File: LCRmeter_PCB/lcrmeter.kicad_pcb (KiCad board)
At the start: 2 copper layers, 64 x 55.2 mm, 70 parts, among them IC1 TPS2116DRLR, J1 LCR_input, J2 LCR_input, J3 Prog_interface, J4 USB_B_Micro, J6 misc, J7 misc, Q1 NX7002BKR, SW1 power, SW2 up, SW3 down, SW4 ok, SW5 back, U1 74LVC1G66, U10 MCP6001-OT, U2 74LVC1G66, U3 OLED, U4 74HC14, U5 MCP6001-OT, U6 STM32G473C_B-C-E_Tx, U7 74LVC1G66, U8 MCP6001-OT, U9 LM1117MP-3.3

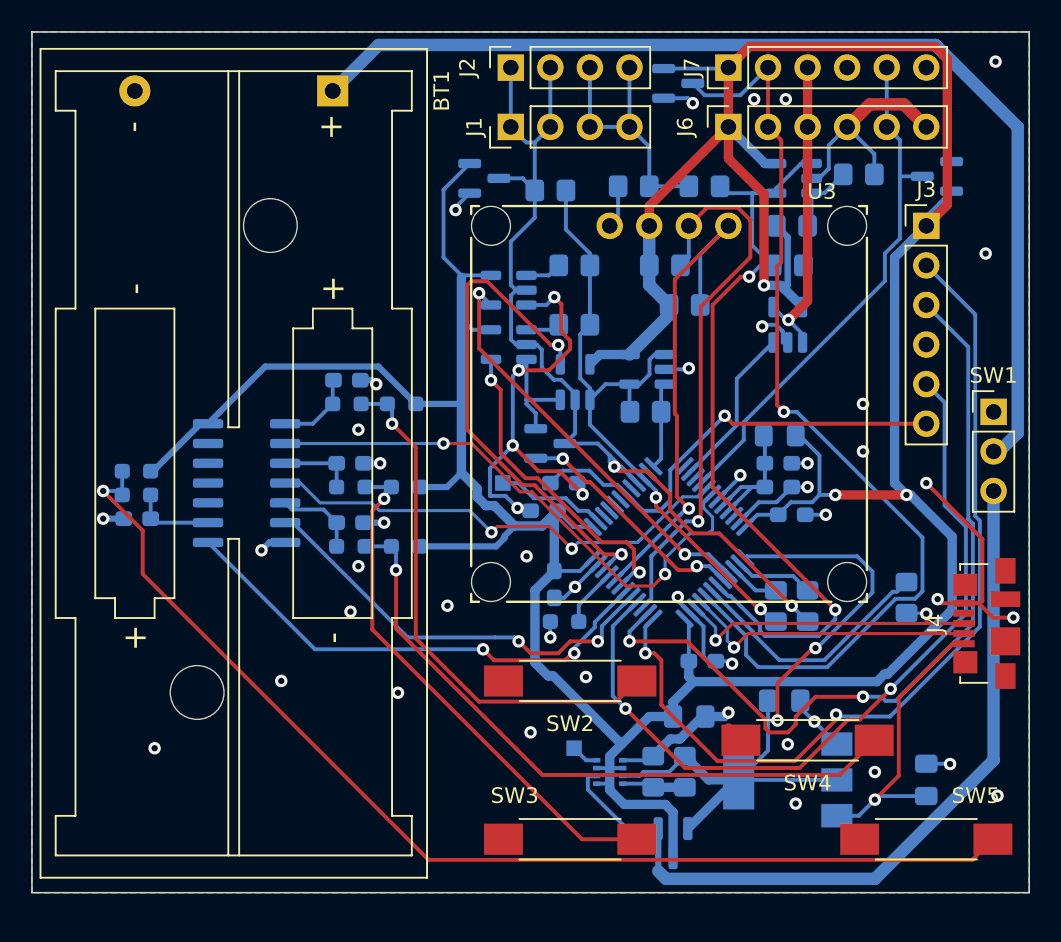
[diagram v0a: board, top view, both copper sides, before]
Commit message: Fix TG connection for Vg; component placement; filter basis
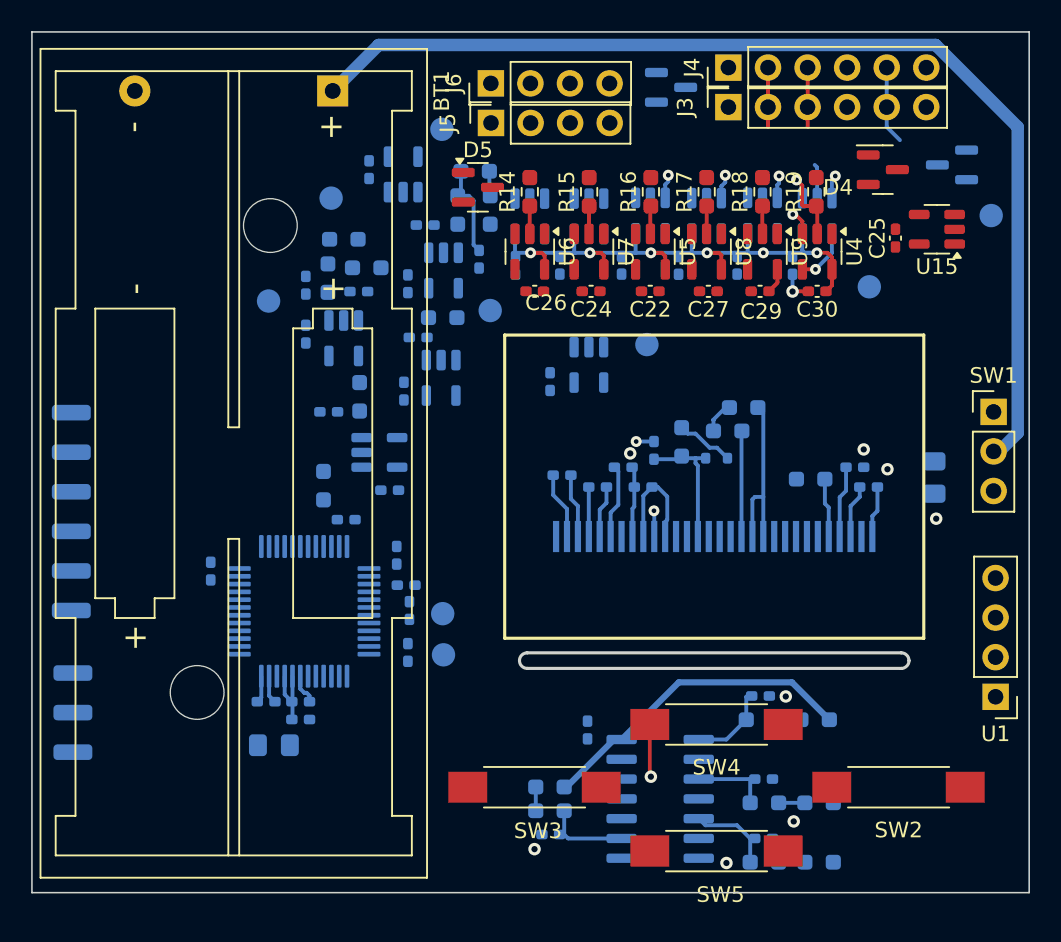
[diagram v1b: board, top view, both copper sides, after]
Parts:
- removed the C18 at (146.1, 115.6)
- removed the C19 at (136.9, 110.5)
- removed D6: BAT54CW, Package_TO_SOT_SMD:SOT-23
- removed IC1: TPS2116DRLR, Library_Loader:SOTFL50P160X60-8N
- removed the J2 at (119.4, 69.8)
- removed the J4 at (149.9, 105.5)
- removed Q1: NX7002BKR, Package_TO_SOT_SMD:SOT-23
- removed the R7 at (138.4, 104.4)
- removed the R8 at (131.8, 77.5)
- removed the U2 at (119.2, 87.6)
- removed the U3 at (133.3, 80.0)
- added C10: 1u, Capacitor_SMD:C_0402_1005Metric_Pad0.74x0.62mm_HandSolder, B.Cu at (125.0, 96.8)
- added C11: 1u, Capacitor_SMD:C_0402_1005Metric_Pad0.74x0.62mm_HandSolder, B.Cu at (126.6, 95.5)
- added C12: 2u2, Capacitor_SMD:C_0402_1005Metric_Pad0.74x0.62mm_HandSolder, B.Cu at (141.5, 95.5)
- added C13: 1u, Capacitor_SMD:C_0402_1005Metric_Pad0.74x0.62mm_HandSolder, B.Cu at (127.9, 96.8)
- added C14: 2u2, Capacitor_SMD:C_0402_1005Metric_Pad0.74x0.62mm_HandSolder, B.Cu at (142.3, 96.8)
- added C20: 100n, Capacitor_SMD:C_0402_1005Metric_Pad0.74x0.62mm_HandSolder, B.Cu at (112.5, 90.6)
- added C21: 100n, Capacitor_SMD:C_0402_1005Metric_Pad0.74x0.62mm_HandSolder, B.Cu at (124.3, 112.4)
- added C22: 100n, Capacitor_SMD:C_0402_1005Metric_Pad0.74x0.62mm_HandSolder, F.Cu at (128.3, 84.2)
- added C23: 100n, Capacitor_SMD:C_0402_1005Metric_Pad0.74x0.62mm_HandSolder, B.Cu at (121.9, 90.0)
- added C24: 100n, Capacitor_SMD:C_0402_1005Metric_Pad0.74x0.62mm_HandSolder, F.Cu at (124.5, 84.2)
- added C25: 100n, Capacitor_SMD:C_0402_1005Metric_Pad0.74x0.62mm_HandSolder, F.Cu at (144.1, 80.8)
- added C26: 100n, Capacitor_SMD:C_0402_1005Metric_Pad0.74x0.62mm_HandSolder, F.Cu at (120.9, 84.2)
- added C27: 100n, Capacitor_SMD:C_0402_1005Metric_Pad0.74x0.62mm_HandSolder, F.Cu at (132.1, 84.2)
- added C28: 100n, Capacitor_SMD:C_0402_1005Metric_Pad0.74x0.62mm_HandSolder, B.Cu at (112.8, 83.7)
- added C29: 100n, Capacitor_SMD:C_0402_1005Metric_Pad0.74x0.62mm_HandSolder, F.Cu at (135.4, 84.2)
- added C30: 100n, Capacitor_SMD:C_0402_1005Metric_Pad0.74x0.62mm_HandSolder, F.Cu at (139.0, 84.2)
- added C31: 220p, Capacitor_SMD:C_0402_1005Metric_Pad0.74x0.62mm_HandSolder, B.Cu at (113.9, 80.0)
- added C32: 1n, Capacitor_SMD:C_0402_1005Metric_Pad0.74x0.62mm_HandSolder, B.Cu at (117.3, 82.2)
- added C33: 220p, Capacitor_SMD:C_0402_1005Metric_Pad0.74x0.62mm_HandSolder, B.Cu at (109.6, 84.2)
- added C34: 1n, Capacitor_SMD:C_0402_1005Metric_Pad0.74x0.62mm_HandSolder, B.Cu at (106.2, 83.8)
- added C35: 1n, Capacitor_SMD:C_0402_1005Metric_Pad0.74x0.62mm_HandSolder, B.Cu at (113.4, 87.2)
- added C36: 1n, Capacitor_SMD:C_0402_1005Metric_Pad0.74x0.62mm_HandSolder, B.Cu at (107.7, 91.9)
- added C37: 1n, Capacitor_SMD:C_0402_1005Metric_Pad0.74x0.62mm_HandSolder, B.Cu at (112.9, 104.7)
- added C38: 1n, Capacitor_SMD:C_0402_1005Metric_Pad0.74x0.62mm_HandSolder, B.Cu at (112.8, 107.4)
- added C39: 100n, Capacitor_SMD:C_0402_1005Metric_Pad0.74x0.62mm_HandSolder, B.Cu at (106.2, 87.0)
- added C40: 100n, Capacitor_SMD:C_0402_1005Metric_Pad0.74x0.62mm_HandSolder, B.Cu at (111.6, 97.0)
- added C41: 100n, Capacitor_SMD:C_0402_1005Metric_Pad0.74x0.62mm_HandSolder, B.Cu at (133.9, 82.5)
- added C42: 100n, Capacitor_SMD:C_0402_1005Metric_Pad0.74x0.62mm_HandSolder, B.Cu at (126.5, 82.5)
- added C43: 100n, Capacitor_SMD:C_0402_1005Metric_Pad0.74x0.62mm_HandSolder, B.Cu at (122.5, 82.5)
- added C44: 100n, Capacitor_SMD:C_0402_1005Metric_Pad0.74x0.62mm_HandSolder, B.Cu at (130.1, 82.5)
- added C45: 100n, Capacitor_SMD:C_0402_1005Metric_Pad0.74x0.62mm_HandSolder, B.Cu at (137.5, 82.5)
- added C46: 100n, Capacitor_SMD:C_0402_1005Metric_Pad0.74x0.62mm_HandSolder, B.Cu at (119.7, 82.5)
- added C47: 100n, Capacitor_SMD:C_0402_1005Metric_Pad0.74x0.62mm_HandSolder, B.Cu at (110.3, 76.4)
- added C6: 2u2, Capacitor_SMD:C_0402_1005Metric_Pad0.74x0.62mm_HandSolder, B.Cu at (128.6, 94.4)
- added C9: 1u, Capacitor_SMD:C_0402_1005Metric_Pad0.74x0.62mm_HandSolder, B.Cu at (122.7, 96.0)
- added D1: 1N4148WT, Diode_SMD:D_SOD-523, B.Cu at (132.6, 94.9)
- added D5: BAT54S, Package_TO_SOT_SMD:SOT-23, F.Cu at (117.3, 77.5)
- added DS1: OLED-128O064D, Display:OLED-128O064D, B.Cu at (132.4, 99.9)
- added J5: LCR_input, Connector_PinSocket_2.54mm:PinSocket_1x04_P2.54mm_Vertical, F.Cu at (118.1, 73.4)
- added J6: LCR_input, Connector_PinHeader_2.54mm:PinHeader_1x04_P2.54mm_Vertical, F.Cu at (118.1, 70.9)
- added R2: 10k, Resistor_SMD:R_0603_1608Metric_Pad0.98x0.95mm_HandSolder, B.Cu at (133.3, 93.2)
- added R26: 649, Resistor_SMD:R_0603_1608Metric_Pad0.98x0.95mm_HandSolder, B.Cu at (115.0, 85.9)
- added R27: 649, Resistor_SMD:R_0603_1608Metric_Pad0.98x0.95mm_HandSolder, B.Cu at (109.7, 91.0)
- added R4: 400k, Resistor_SMD:R_0603_1608Metric_Pad0.98x0.95mm_HandSolder, B.Cu at (138.6, 96.3)
- added TP1: TestPoint, TestPoint:TestPoint_Pad_D1.5mm, B.Cu at (115.0, 73.8)
- added TP2: TestPoint, TestPoint:TestPoint_Pad_D1.5mm, B.Cu at (107.8, 78.2)
- added TP5: ~, TestPoint:TestPoint_Pad_D1.5mm, B.Cu at (128.1, 87.6)
- added TP6: ~, TestPoint:TestPoint_Pad_D1.5mm, B.Cu at (142.4, 83.9)
- added TP7: TestPoint, TestPoint:TestPoint_Pad_D1.5mm, B.Cu at (115.1, 107.5)
- added TP8: TestPoint, TestPoint:TestPoint_Pad_D1.5mm, B.Cu at (115.0, 104.9)
- added TP9: ~, TestPoint:TestPoint_Pad_D1.5mm, B.Cu at (150.2, 79.3)
- added U11: LT6202, Package_TO_SOT_SMD:SOT-23-5, B.Cu at (108.7, 87.2)
- added U12: LMH6645, Package_TO_SOT_SMD:SOT-23-5, B.Cu at (124.4, 88.9)
- added U13: LT6202, Package_TO_SOT_SMD:SOT-23-5, B.Cu at (114.9, 89.8)
- added U14: LT6202, Package_TO_SOT_SMD:SOT-23-5, B.Cu at (110.9, 94.6)
- added U15: LMH6645, Package_TO_SOT_SMD:SOT-23-5, F.Cu at (146.7, 80.2)
- added U16: 74LVC1G66, Package_TO_SOT_SMD:SOT-23-5, B.Cu at (120.6, 79.4)
- added U17: 74LVC1G66, Package_TO_SOT_SMD:SOT-23-5, B.Cu at (124.4, 79.4)
- added U18: 74LVC1G66, Package_TO_SOT_SMD:SOT-23-5, B.Cu at (128.3, 79.3)
- added U19: 74LVC1G66, Package_TO_SOT_SMD:SOT-23-5, B.Cu at (131.9, 79.4)
- added U20: 74LVC1G66, Package_TO_SOT_SMD:SOT-23-5, B.Cu at (135.5, 79.3)
- added U21: 74LVC1G66, Package_TO_SOT_SMD:SOT-23-5, B.Cu at (139.0, 79.4)
- added U22: 74LVC1G66, Package_TO_SOT_SMD:SOT-23-5, B.Cu at (112.5, 76.7)
- added U4: 74LVC1G66, Package_TO_SOT_SMD:SOT-23-5, F.Cu at (139.0, 81.7)
- added U6: 74LVC1G66, Package_TO_SOT_SMD:SOT-23-5, F.Cu at (120.6, 81.7)
- C15: renamed from C12; footprint Capacitor_SMD:C_0603_1608Metric_Pad1.08x0.95mm_HandSolder -> Capacitor_SMD:C_0402_1005Metric_Pad0.74x0.62mm_HandSolder
- C16: renamed from C13; footprint Capacitor_SMD:C_0603_1608Metric_Pad1.08x0.95mm_HandSolder -> Capacitor_SMD:C_0402_1005Metric_Pad0.74x0.62mm_HandSolder
- C17: renamed from C14; footprint Capacitor_SMD:C_0603_1608Metric_Pad1.08x0.95mm_HandSolder -> Capacitor_SMD:C_0402_1005Metric_Pad0.74x0.62mm_HandSolder
- C18: renamed from C15; footprint Capacitor_SMD:C_0603_1608Metric_Pad1.08x0.95mm_HandSolder -> Capacitor_SMD:C_0402_1005Metric_Pad0.74x0.62mm_HandSolder
- C19: renamed from C10; footprint Capacitor_SMD:C_0603_1608Metric_Pad1.08x0.95mm_HandSolder -> Capacitor_SMD:C_0402_1005Metric_Pad0.74x0.62mm_HandSolder
- C2: renamed from C9; value 100n -> 2u2; footprint Capacitor_SMD:C_0603_1608Metric_Pad1.08x0.95mm_HandSolder -> Capacitor_SMD:C_0402_1005Metric_Pad0.74x0.62mm_HandSolder
- C3, C4: value 100n -> 2u2; footprint Capacitor_SMD:C_0603_1608Metric_Pad1.08x0.95mm_HandSolder -> Capacitor_SMD:C_0402_1005Metric_Pad0.74x0.62mm_HandSolder
- C5, C7: footprint Capacitor_SMD:C_0603_1608Metric_Pad1.08x0.95mm_HandSolder -> Capacitor_SMD:C_0402_1005Metric_Pad0.74x0.62mm_HandSolder
- C8: renamed from C11; footprint Capacitor_SMD:C_0603_1608Metric_Pad1.08x0.95mm_HandSolder -> Capacitor_SMD:C_0402_1005Metric_Pad0.74x0.62mm_HandSolder
- D4, U7: moved to F.Cu
- J1: value LCR_input -> UART; footprint Connector_PinHeader_2.54mm:PinHeader_1x04_P2.54mm_Vertical -> Connector_Harwin:Harwin_M20-89003xx_1x03_P2.54mm_Horizontal; moved to B.Cu
- J2: renamed from J3; footprint Connector_PinHeader_2.54mm:PinHeader_1x06_P2.54mm_Vertical -> Connector_Harwin:Harwin_M20-89006xx_1x06_P2.54mm_Horizontal; moved to B.Cu
- R1: value 100 -> 10k; footprint Resistor_SMD:R_0805_2012Metric_Pad1.20x1.40mm_HandSolder -> Resistor_SMD:R_0603_1608Metric_Pad0.98x0.95mm_HandSolder
- R14: value 1k5 -> 22; footprint Resistor_SMD:R_0805_2012Metric_Pad1.20x1.40mm_HandSolder -> Resistor_SMD:R_0603_1608Metric_Pad0.98x0.95mm_HandSolder; moved to F.Cu
- R15: value 1k5 -> 47; footprint Resistor_SMD:R_0805_2012Metric_Pad1.20x1.40mm_HandSolder -> Resistor_SMD:R_0603_1608Metric_Pad0.98x0.95mm_HandSolder; moved to F.Cu
- R16: value 1k5 -> 100; footprint Resistor_SMD:R_0805_2012Metric_Pad1.20x1.40mm_HandSolder -> Resistor_SMD:R_0603_1608Metric_Pad0.98x0.95mm_HandSolder; moved to F.Cu
- R17: value 0 -> 220; footprint Resistor_SMD:R_0805_2012Metric_Pad1.20x1.40mm_HandSolder -> Resistor_SMD:R_0603_1608Metric_Pad0.98x0.95mm_HandSolder; moved to F.Cu
- R18: value 2k -> 470; footprint Resistor_SMD:R_0805_2012Metric_Pad1.20x1.40mm_HandSolder -> Resistor_SMD:R_0603_1608Metric_Pad0.98x0.95mm_HandSolder; moved to F.Cu
- R19: value 500 -> 1k; footprint Resistor_SMD:R_0805_2012Metric_Pad1.20x1.40mm_HandSolder -> Resistor_SMD:R_0603_1608Metric_Pad0.98x0.95mm_HandSolder; moved to F.Cu
- R20, R21: value 0 -> 976; footprint Resistor_SMD:R_0805_2012Metric_Pad1.20x1.40mm_HandSolder -> Resistor_SMD:R_0603_1608Metric_Pad0.98x0.95mm_HandSolder
- R22, R23: value 10k -> 2k; footprint Resistor_SMD:R_0805_2012Metric_Pad1.20x1.40mm_HandSolder -> Resistor_SMD:R_0603_1608Metric_Pad0.98x0.95mm_HandSolder
- R24: value 1k5 -> 0; footprint Resistor_SMD:R_0805_2012Metric_Pad1.20x1.40mm_HandSolder -> Resistor_SMD:R_0603_1608Metric_Pad0.98x0.95mm_HandSolder
- R25: value 2k2 -> 0; footprint Resistor_SMD:R_0805_2012Metric_Pad1.20x1.40mm_HandSolder -> Resistor_SMD:R_0603_1608Metric_Pad0.98x0.95mm_HandSolder
- R3: value 0 -> 400k; footprint Resistor_SMD:R_0805_2012Metric_Pad1.20x1.40mm_HandSolder -> Resistor_SMD:R_0603_1608Metric_Pad0.98x0.95mm_HandSolder
- TP3, TP4: footprint TestPoint:TestPoint_Pad_1.0x1.0mm -> TestPoint:TestPoint_Pad_D1.5mm
- U1: value 74LVC1G66 -> Mylibrary_OLED; footprint Package_TO_SOT_SMD:SOT-23-5 -> Connector_PinHeader_2.54mm:PinHeader_1x04_P2.54mm_Vertical; moved to F.Cu
- U10: value MCP6001-OT -> LT6202
- U5, U8: value MCP6001-OT -> 74LVC1G66; moved to F.Cu
- U9: value LM1117MP-3.3 -> 74LVC1G66; footprint Package_TO_SOT_SMD:SOT-223-3_TabPin2 -> Package_TO_SOT_SMD:SOT-23-5; moved to F.Cu
- moved J2 63.1 mm to (85.6, 98.3), turned to 180 degrees
- moved J1 50.4 mm to (85.8, 111.3), turned to 180 degrees
- moved U1 40.7 mm to (150.5, 110.2)
- moved R25 38.3 mm to (110.1, 82.7), turned to 0 degrees
- moved L1 38.1 mm to (104.2, 113.3), turned to 0 degrees
- moved R24 37.5 mm to (118.1, 79.0)
- moved C3 35.8 mm to (103.7, 110.6)
- moved C8 34.8 mm to (105.9, 111.7)
- moved TP4 34.8 mm to (103.8, 84.8)
- moved R23 34.7 mm to (107.6, 83.4), turned to -90 degrees
- moved U9 33.9 mm to (135.5, 81.7), turned to -90 degrees
- moved C7 33.6 mm to (105.9, 110.6)
- moved C16 33.4 mm to (121.9, 119.1)
- moved C17 33.4 mm to (135.4, 110.2)
- moved R10 33.4 mm to (121.9, 117.6)
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- renumbered C8 to C1, D3 to D2, D2 to D3, J6 to J3, J7 to J4, L2 to L1, R11 to R10, R12 to R11, R13 to R12, R2 to R13, R4 to R5, R5 to R6, R6 to R7, R9 to R8, R10 to R9, SW4 to SW2, SW5 to SW3, SW2 to SW4, SW3 to SW5, U4 to U2, U6 to U3
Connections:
- C1 pad 1: VCC -> Net-(BT1-+)
- D4 pad 3: /ADC_2 -> /WAVE_OUT
- J1 pad 1: /ADC_2 -> GND
- J1 pad 2: /ADC_2 -> /USART_TX
- J1 pad 3: Net-(J1-Pin_3) -> /USART_RX
- J2 pad 2: Net-(J3-Pin_2) -> Net-(J2-Pin_2)
- J2 pad 3: Net-(J3-Pin_3) -> GND
- J2 pad 4: GND -> Net-(J2-Pin_4)
- J2 pad 5: /SWO -> /RST
- J2 pad 6: /RST -> /SWO
- R1 pad 1: /ADC_1 -> VCC
- R1 pad 2: /ADC_2 -> /SDA
- R14 pad 1: VCC -> Net-(R14-Pad1)
- R14 pad 2: /SDA -> /Vx
- R15 pad 1: /USB_EN -> Net-(R15-Pad1)
- R15 pad 2: /USB_+ -> /Vx
- R16 pad 1: VCC -> Net-(R16-Pad1)
- R16 pad 2: /SCL -> /Vx
- R17 pad 1: Net-(J1-Pin_3) -> Net-(R17-Pad1)
- R17 pad 2: GND -> /Vx
- R18 pad 1: /ADC_1 -> Net-(R18-Pad1)
- R18 pad 2: Net-(R18-Pad2) -> /Vx
- R19 pad 1: /ADC_1 -> Net-(R19-Pad1)
- R19 pad 2: Net-(R19-Pad2) -> /Vx
- R20 pad 1: /DAC_UNBUFFERED -> /analog signals/Vg
- R20 pad 2: /ADC_1 -> Net-(C32-Pad1)
- R21 pad 1: Net-(U8-+) -> Net-(R21-Pad1)
- R21 pad 2: +1V5 -> Net-(C34-Pad1)
- R22 pad 1: Net-(U8-+) -> Net-(C32-Pad1)
- R22 pad 2: VCC -> Net-(U10-+)
- R23 pad 1: GND -> Net-(C34-Pad1)
- R23 pad 2: Net-(U8-+) -> Net-(U11-+)
- R24 pad 1: GND -> /analog signals/Vg
- R24 pad 2: Net-(IC1-PR1) -> /Vg_FILTERED
- R25 pad 1: Net-(IC1-PR1) -> Net-(R21-Pad1)
- R25 pad 2: /V_USB -> /Vx_FILTERED
- R3 pad 1: /ADC_1 -> /Display_VCC
- R3 pad 2: /ADC_1b -> Net-(D1-A)
- TP3 pad 1: /EVENTOUT -> Net-(U10--)
- U1 pad 1: Net-(R19-Pad2) -> /SDA
- U1 pad 2: /ADC_2 -> /SCL
- U1 pad 3: GND -> VCC
- U1 pad 4: /EN_PATH_1 -> GND
- U10 pad 1: /WAVE_OUT -> Net-(U10--)
- U10 pad 3: /WAVE_OUT_UNBUFFERED -> Net-(U10-+)
- U10 pad 4: /WAVE_OUT -> Net-(U10--)
- U3 pad 10: /ADC_1 -> /Vg_FILTERED
- U3 pad 16: /OSCILLOSCOPE_IN -> unconnected-(U3-PB0-Pad16)
- U3 pad 2: /EVENTOUT -> unconnected-(U3-PC13-Pad2)
- U3 pad 25: /V_USB -> /EN_PATH_6
- U3 pad 26: /ADC_2b -> /OSCILLOSCOPE_IN
- U3 pad 27: /ADC_1b -> /EN_PATH_5
- U3 pad 29: /RES_CALIBRATION -> /EN_PATH_4
- U3 pad 30: +1V5 -> unconnected-(U3-PA8-Pad30)
- U3 pad 31: /USB_EN -> unconnected-(U3-PA9-Pad31)
- U3 pad 32: /PWM_OUT -> /USART_RX
- U3 pad 33: /USB_- -> /USART_TX
- U3 pad 34: /USB_+ -> /PWM_OUT
- U3 pad 37: Net-(J3-Pin_2) -> Net-(J2-Pin_4)
- U3 pad 38: Net-(J3-Pin_3) -> Net-(J2-Pin_2)
- U3 pad 9: /ADC_2 -> /Vx_FILTERED
- U5 pad 1: /ADC_1 -> /analog signals/DAC_BUFFERED
- U5 pad 2: GND -> Net-(R16-Pad1)
- U5 pad 3: /DAC_UNBUFFERED -> GND
- U5 pad 4: /ADC_1 -> /EN_PATH_3
- U7 pad 1: /ADC_1 -> /analog signals/DAC_BUFFERED
- U7 pad 2: /ADC_2 -> Net-(R15-Pad1)
- U7 pad 4: /EN_PATH_3 -> /EN_PATH_2
- U8 pad 1: +1V5 -> /analog signals/DAC_BUFFERED
- U8 pad 2: GND -> Net-(R17-Pad1)
- U8 pad 3: Net-(U8-+) -> GND
- U8 pad 4: +1V5 -> /EN_PATH_4
- U9 pad 1: GND -> /analog signals/DAC_BUFFERED
- U9 pad 2: /V_USB -> Net-(R18-Pad1)
- U9 pad 3: VBUS -> GND
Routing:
- net VCC: track 269.2 -> 76.2 mm, vias 3 -> 6
- net GND: track 118.6 -> 27.7 mm, vias 48 -> 17
- net Net-(R10-Pad2): track 72.0 -> 1.52 mm, vias 1 -> 0
- net /ADC_2: track 64.2 -> 0.00 mm, vias 2 -> 0
- net /PWM_OUT: track 62.8 -> 3.81 mm, vias 1 -> 0
- net Net-(J3-Pin_2): track 56.9 -> 0.00 mm, vias 2 -> 0
- net Net-(J3-Pin_3): track 52.2 -> 0.00 mm, vias 2 -> 0
- net +BATT: track 51.9 -> 0.00 mm
- net /SWO: track 51.1 -> 0.00 mm, vias 2 -> 0
- net +1V5: track 50.0 -> 0.00 mm, vias 2 -> 0
- net /V_USB: track 46.8 -> 0.00 mm, vias 2 -> 0
- net /ADC_1: track 42.3 -> 0.00 mm, vias 2 -> 0
- net Net-(R5-Pad2): track 42.6 -> 1.68 mm, vias 1 -> 0
- net /BUTTON_+: track 36.1 -> 0.00 mm, vias 2 -> 0
- net /EN_PATH_3: track 33.0 -> 0.00 mm, vias 2 -> 0
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- removed copper zone on B.Cu, net GND
- removed copper zone on F.Cu, net GND
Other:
- outline, holes or cut-outs redrawn
- copper layers 2 -> 4

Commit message: PCB and schematic update for next version
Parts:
- added C48: 10u, Capacitor_SMD:C_0805_2012Metric_Pad1.18x1.45mm_HandSolder, B.Cu at (104.2, 90.5)
- added H1: M, MountingHole:MountingHole_3.2mm_M3_ISO14580, F.Cu at (149.2, 86.5)
- C1: value 10u -> 20u
- C25, D4, U15: moved to B.Cu
- moved TP5 12.0 mm to (117.5, 93.2)
- moved TP9 10.3 mm to (143.7, 87.2)
- moved C1 7.80 mm to (139.6, 92.7), turned to 0 degrees
- moved C21 5.11 mm to (129.3, 111.5), turned to 180 degrees
- moved C23 4.35 mm to (124.1, 86.2), turned to 180 degrees
- moved C25 3.80 mm to (147.6, 79.3), turned to -90 degrees
- moved C47 3.30 mm to (112.2, 73.8), turned to 180 degrees
- moved C17 3.20 mm to (135.4, 113.4)
- moved C35 1.75 mm to (115.2, 87.5)
- moved R27 1.71 mm to (108.0, 91.3)
- moved U15 1.71 mm to (145.0, 80.4), turned to 90 degrees
- moved C36 1.69 mm to (107.5, 93.6)
- moved C44 1.48 mm to (131.5, 82.0), turned to 180 degrees
- moved C42 1.48 mm to (127.9, 82.0), turned to 180 degrees
- moved C43 1.44 mm to (123.9, 82.1), turned to 180 degrees
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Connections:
- C1 pad 1: Net-(BT1-+) -> VCC
- J1 pad 2: /USART_TX -> /USART_RX
- J1 pad 3: /USART_RX -> /USART_TX
- SW1 pad 3: +BATT -> VCC
- U2 pad 2: /BUTTON_+ -> /BUTTON_UP
- U2 pad 4: /BUTTON_- -> /BUTTON_DOWN
- U3 pad 10: /Vg_FILTERED -> unconnected-(U3-PA2-Pad10)
- U3 pad 11: unconnected-(U3-PA3-Pad11) -> /Vg_FILTERED
- U3 pad 15: unconnected-(U3-PA7-Pad15) -> /BUTTON_UP
- U3 pad 16: unconnected-(U3-PB0-Pad16) -> /BUTTON_DOWN
- U3 pad 17: /BUTTON_- -> /BUTTON_BACK
- U3 pad 18: /BUTTON_+ -> /BUTTON_OK
- U3 pad 28: /EN_PATH_1 -> /EN_PATH_4
- U3 pad 29: /EN_PATH_4 -> /EN_PATH_3
- U3 pad 30: unconnected-(U3-PA8-Pad30) -> /EN_PATH_2
- U3 pad 31: unconnected-(U3-PA9-Pad31) -> /USART_TX
- U3 pad 33: /USART_TX -> /PWM_OUT
- U3 pad 34: /PWM_OUT -> /EN_PATH_1
- U3 pad 41: /BUTTON_OK -> unconnected-(U3-PB4-Pad41)
- U3 pad 42: /BUTTON_BACK -> unconnected-(U3-PB5-Pad42)
- U3 pad 43: /EN_PATH_2 -> unconnected-(U3-PB6-Pad43)
- U3 pad 46: /EN_PATH_3 -> unconnected-(U3-PB9-Pad46)
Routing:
- net VCC: track 76.2 -> 404.9 mm, vias 6 -> 19
- net GND: track 27.7 -> 147.2 mm, vias 17 -> 49
- net /OSCILLOSCOPE_IN: track 5.01 -> 102.1 mm
- net /PWM_OUT: track 3.81 -> 69.8 mm, vias 0 -> 2
- net /SDA: track 11.6 -> 75.7 mm, vias 0 -> 2
- net /SCL: track 6.79 -> 66.5 mm, vias 0 -> 3
- net /BUTTON_DOWN: track 0.00 -> 58.1 mm, vias 0 -> 2
- net /WAVE_OUT_UNBUFFERED: track 0.00 -> 57.5 mm
- net Net-(BT1-+): track 68.7 -> 123.4 mm, vias 0 -> 6
- net /EN_PATH_5: track 0.00 -> 50.5 mm, vias 0 -> 3
- net /EN_PATH_6: track 3.62 -> 54.0 mm, vias 1 -> 3
- net /EN_PATH_4: track 0.00 -> 47.5 mm, vias 0 -> 3
- net /EN_PATH_3: track 0.00 -> 43.6 mm, vias 0 -> 3
- net /Vx: track 0.00 -> 42.6 mm
- net /EN_PATH_2: track 0.00 -> 41.8 mm, vias 0 -> 3
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- added copper zone on In1.Cu, net GND
- added copper zone on In2.Cu, net GND
- added copper zone on B.Cu, net Net-(BT1-+)
- added copper zone on F.Cu, net Net-(BT1-+)
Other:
- board text added: "LCRmeter v3.1 2026 Rafał Mazurkiewicz"
- board text removed: "LCRmeter v3 2023 Rafał Mazurkiewicz"

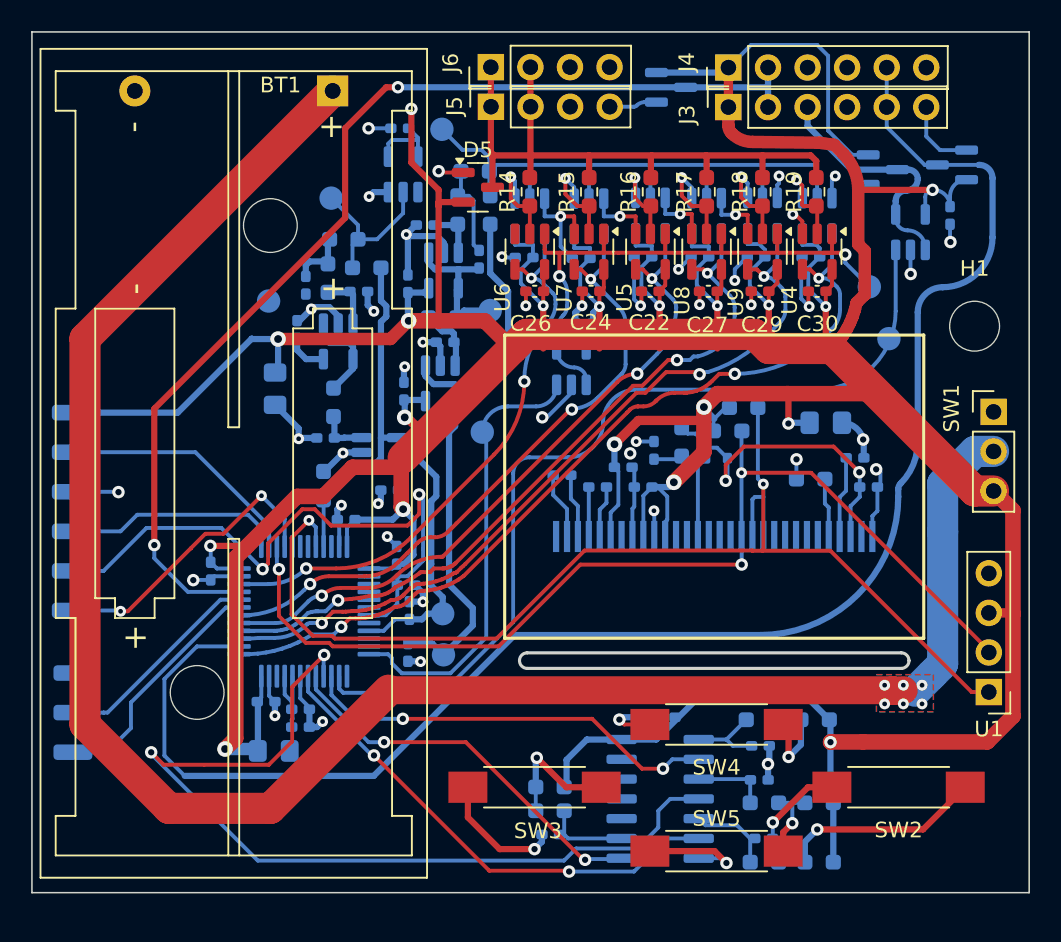
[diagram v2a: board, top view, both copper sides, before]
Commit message: fix pcb and oled connection
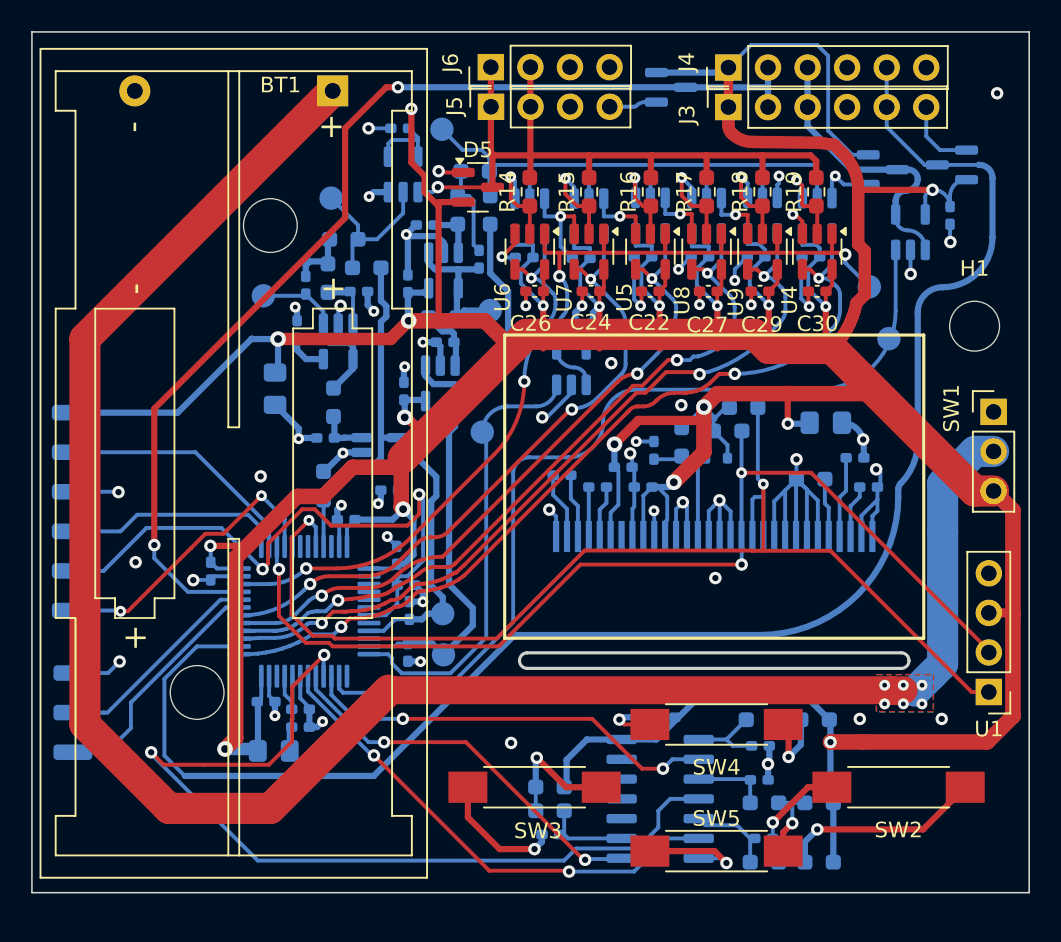
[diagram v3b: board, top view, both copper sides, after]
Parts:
- moved TP4 0.47 mm to (103.5, 84.5)
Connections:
- D1 pad 1: /Display_VCC -> VCC
- R3 pad 1: /Display_VCC -> VCC
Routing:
- net GND: track 147.2 -> 190.6 mm, vias 49 -> 63
- net /Display_VCC: track 20.4 -> 3.42 mm, vias 2 -> 0
- net Net-(U11--): track 6.18 -> 11.3 mm
- net /Vx: track 42.6 -> 47.5 mm, vias 0 -> 1
- net VCC: track 404.9 -> 409.1 mm
- net /Vg_FILTERED: track 37.5 -> 40.1 mm
- net /WAVE_OUT: track 16.1 -> 18.6 mm
- net VDDA: track 5.59 -> 7.18 mm
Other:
- board text added: "CLK"
- board text added: "GND"
- board text added: "IO"
- board text added: "RST"
- board text added: "RX"
- board text added: "SWO"
- board text added: "TX"
- board text added: "VCC"
